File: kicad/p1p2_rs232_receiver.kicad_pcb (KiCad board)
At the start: 2 copper layers, 64.5 x 28 mm, 46 parts, among them J101 Screw_Terminal_01x03, J102 USB_B_Mini, Q101 Q_NPN_CBE, U101 MAX22088, U102 ISO7342C, U103 CY7C65213-32LTXI

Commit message: Update PCB
- Increase dimension for easy DIN rail mounting
- Add more labels
- Move parts to increase ground plane

Signed-off-by: Patrick Rudolph <siro@das-labor.org>
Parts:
- J101: value Screw_Terminal_01x03 -> TE Connectivity 1776112-3
- moved C109 12.6 mm to (135.7, 130.8)
- moved D106 5.76 mm to (150.8, 119.5), turned to 0 degrees
- moved R108 5.62 mm to (142.4, 116.5)
- moved J101 4.96 mm to (165.0, 123.5)
- moved C105 4.02 mm to (161.2, 117.2)
- moved R107 4.00 mm to (134.5, 125.5), turned to 270 degrees
- moved D105 3.61 mm to (140.0, 126.5), turned to 0 degrees
- moved D103 2.83 mm to (134.8, 119.0), turned to 270 degrees
- moved D102 2.50 mm to (150.8, 131.0)
- moved C107 2.42 mm to (134.4, 124.2)
- moved Q101 2.30 mm to (141.5, 126.9)
- moved R102 2.02 mm to (147.0, 125.0)
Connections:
- U102 pad 7: /~SLEEP -> VBUS
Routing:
- net Net-(C106-Pad1): track 41.0 -> 65.4 mm, vias 0 -> 2
- net /~SLEEP: track 14.5 -> 0.00 mm, vias 1 -> 0
- net VBUS: track 76.7 -> 88.4 mm
- net Net-(C107-Pad1): track 27.0 -> 33.6 mm
- net Net-(U103-Pad5): track 4.56 -> 0.00 mm, vias 1 -> 0
- net Net-(C109-Pad2): track 11.6 -> 7.40 mm
- net Net-(R108-Pad1): track 8.24 -> 4.13 mm
- net Net-(C108-Pad2): track 10.3 -> 14.2 mm
- net Net-(R106-Pad1): track 13.9 -> 17.5 mm
- net Net-(C105-Pad2): track 9.04 -> 12.2 mm
- net +15V: track 8.24 -> 11.0 mm
- net Net-(C107-Pad2): track 34.4 -> 36.6 mm, vias 2 -> 3
- net Net-(C105-Pad1): track 23.4 -> 21.3 mm
- net GND: vias 12 -> 11
- net (no net): vias 0 -> 1
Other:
- board size 64.5 x 28 mm -> 71.8 x 28 mm
- board text added: "36V max"
- board text added: "D1"
- board text added: "D2"

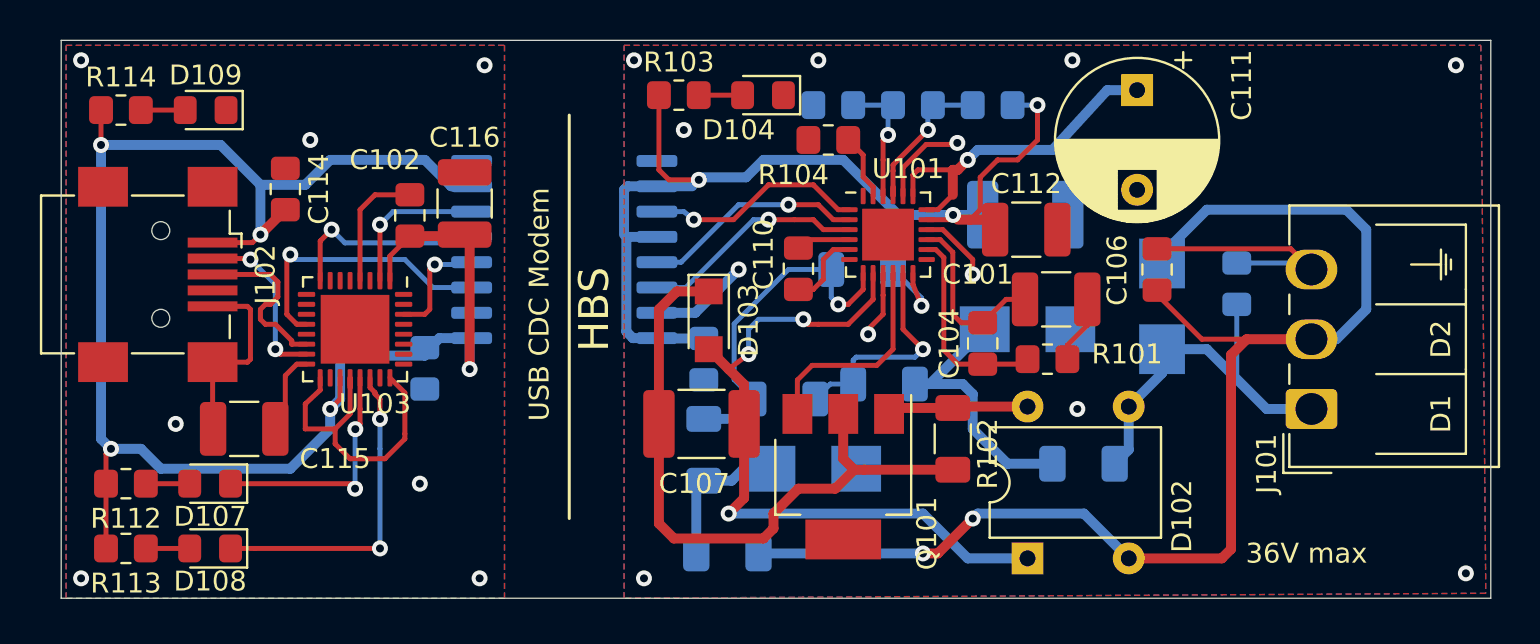
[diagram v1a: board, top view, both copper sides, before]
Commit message: Add 9600baud CTS low pass filter
- Add low pass filter with tRC of 1.2 msec
- Pull CTS low when data is received for easy collision detection

Signed-off-by: Patrick Rudolph <siro@das-labor.org>
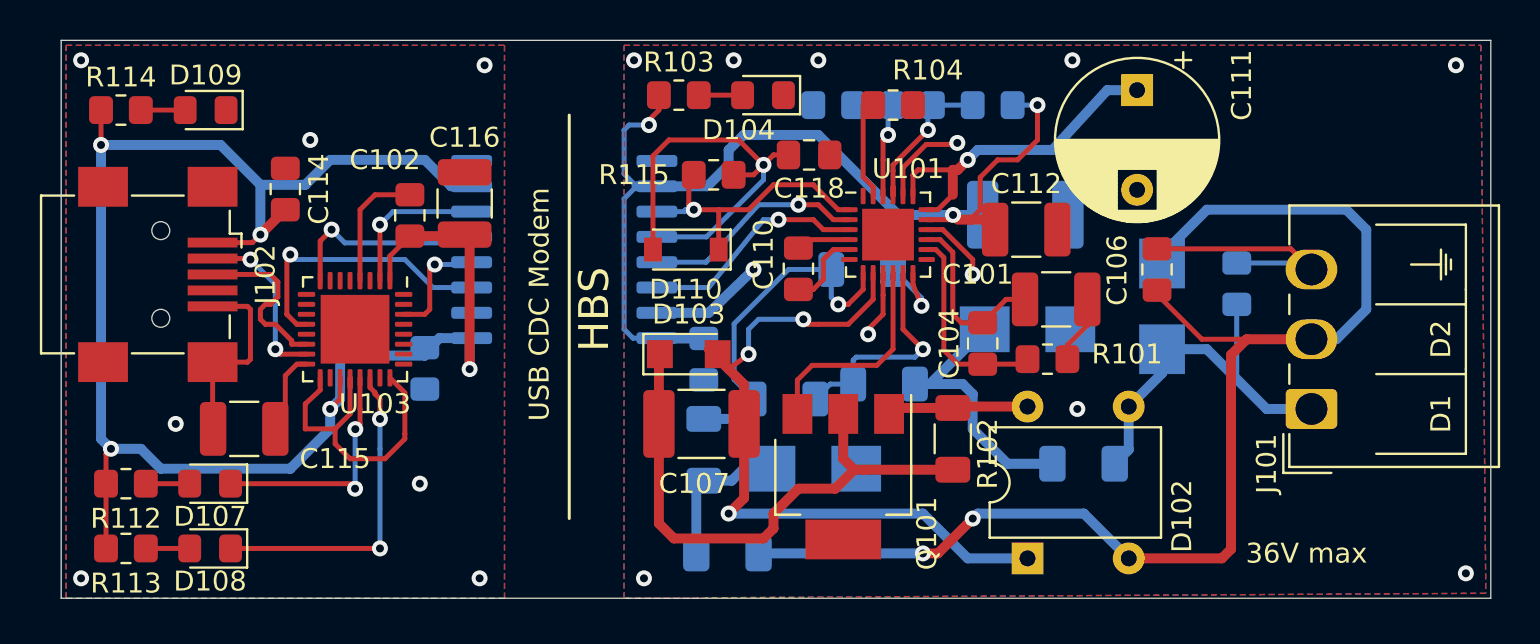
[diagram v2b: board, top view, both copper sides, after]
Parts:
- added C118: 10n, Capacitor_SMD:C_0805_2012Metric_Pad1.18x1.45mm_HandSolder, F.Cu at (139.8, 110.8)
- added D110: D_Schottky, Diode_SMD:D_SOD-123, F.Cu at (133.6, 115.5)
- added R115: 120k, Resistor_SMD:R_0805_2012Metric_Pad1.20x1.40mm_HandSolder, F.Cu at (135.0, 111.8)
- moved R104 3.69 mm to (144.0, 108.2), turned to 0 degrees
- moved D103 1.97 mm to (133.8, 120.8), turned to 0 degrees
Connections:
- U102 pad 12: VCC -> Net-(C118-Pad2)
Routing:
- net Net-(C118-Pad2): track 0.00 -> 21.6 mm, vias 0 -> 1
- net Net-(C107-Pad1): track 33.6 -> 28.5 mm
- net Net-(D110-Pad1): track 11.0 -> 14.7 mm
- net Net-(R104-Pad1): track 3.33 -> 4.77 mm
- net GND: track 16.6 -> 17.4 mm, vias 11 -> 12
- net (no net): vias 1 -> 0
